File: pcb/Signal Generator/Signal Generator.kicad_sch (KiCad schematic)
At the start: 16 parts, among them SW1 SW_Push, SW1 SW_SPDT, U1 STM32F103CBTx, Y1 TG2520SMN_16.0000M-MCGNNM0

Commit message: Updated pcb
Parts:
- removed C9: 1u, symbol Device:C
- removed FB1: FerriteBead, symbol Device:FerriteBead
- removed U1: STM32F103CBTx, Package_QFP:LQFP-48_7x7mm_P0.5mm, symbol MCU_ST_STM32F1:STM32F103CBTx
- added C? (x2): 1u, symbol Device:C
- added R?: 10K, symbol Device:R
- added R? (x6): R, symbol Device:R
- added R?: 100K, symbol Device:R
- added U1: STM32F071RBTx, Package_QFP:LQFP-64_10x10mm_P0.5mm, symbol MCU_ST_STM32F0:STM32F071RBTx
- added U? (x3): Opamp_Dual, symbol Device:Opamp_Dual
- added U?: TS972IYQT, Signal Generator Components:TS972IYQT, symbol Signal Generator Components:TS972IYQT
- added U?: LDLN030G33R, Signal Generator Components:LDLN030G33R, symbol Signal Generator Components:LDLN030G33R
- C10: value C -> 100n
- C?: renamed from C6; value 4.5u -> 4.7u
- C?: renamed from C5; value 100n -> 4.7u
- renumbered C3 to C?, C4 to C?, C2 to C?, C1 to C?, C7 to C?, C8 to C?
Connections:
- net +3.3VA is gone; now on net +3.3V: C?.1, C?.1
- net +3.3V: now also C?.1, R?.2, R?.2, R?.2, U1.1 (VBAT), U1.13 (VDDA), U1.19 (VDD), U1.32 (VDD), U1.48 (VDDIO2), U1.64 (VDD), U?.5 (OUT), U?.8 (V+)
- net +5V: now also C?.1, R?.2, U?.1 (IN)
- net BOOT0: now also U1.60 (BOOT0)
- net DAC1: now also R?.1, U1.20 (PA4), U?.2 (-)
- net DAC2: now also R?.1, U1.21 (PA5), U?.6 (-)
- net GND: now also C?.2, C?.2, R?.1, R?.1, U1.12 (VSSA), U1.18 (VSS), U1.31 (VSS), U1.47 (VSS), U1.63 (VSS), U?.2 (GND), U?.4 (V-)
- net NRST: now also U1.7 (NRST)
- net OSC_IN: now also U1.5 (PF0)
- net UART1_RX: now also U1.59 (PB7)
- net UART1_TX: now also U1.58 (PB6)
- new net: R?.1, U?.3 (EN)
- new net: R?.1, R?.2, U?.5 (+)
- new net: R?.1, R?.2, U?.3 (+)
- new net: R?.1, U?.4 (PG)
- new net DAC1_OUT: R?.2, R?.2, U?.1, U?.7
- no-connect marks 1 -> 0
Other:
- sheet USB Plugs1 ports: added none; removed USB1_D+, USB1_D-
- note added: "LDO & Decoupling"
- note added: "When buffer is off: DAC output resistance 15k max Output speed follows the RC constant When internal buffer is on: OpAmp configured as an inverting amplifier DAC output resistance almost zero Speed determined by the buffer: T_settling = 4us max (250KHz) The most limiting factor when using only the internal DAC is the output impedance on the pin. To improve the DAC performance an external OpAmp ca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"
- note removed: "Decoupling"
- moved on the sheet: C?

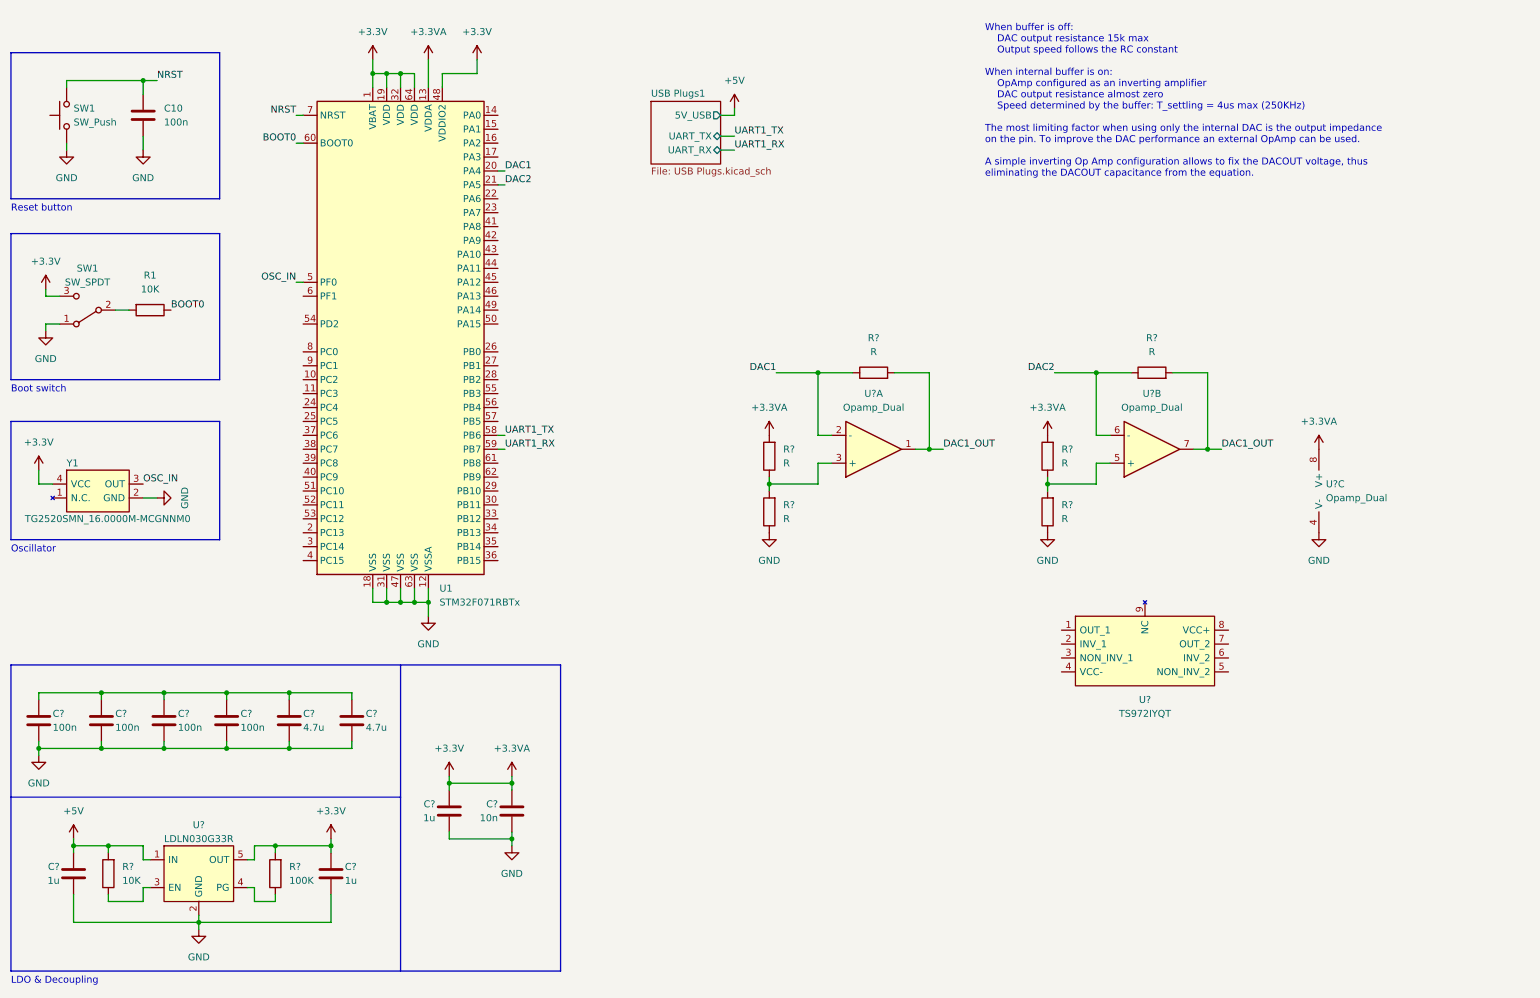
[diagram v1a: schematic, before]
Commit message: Updated schematic with almost final front end
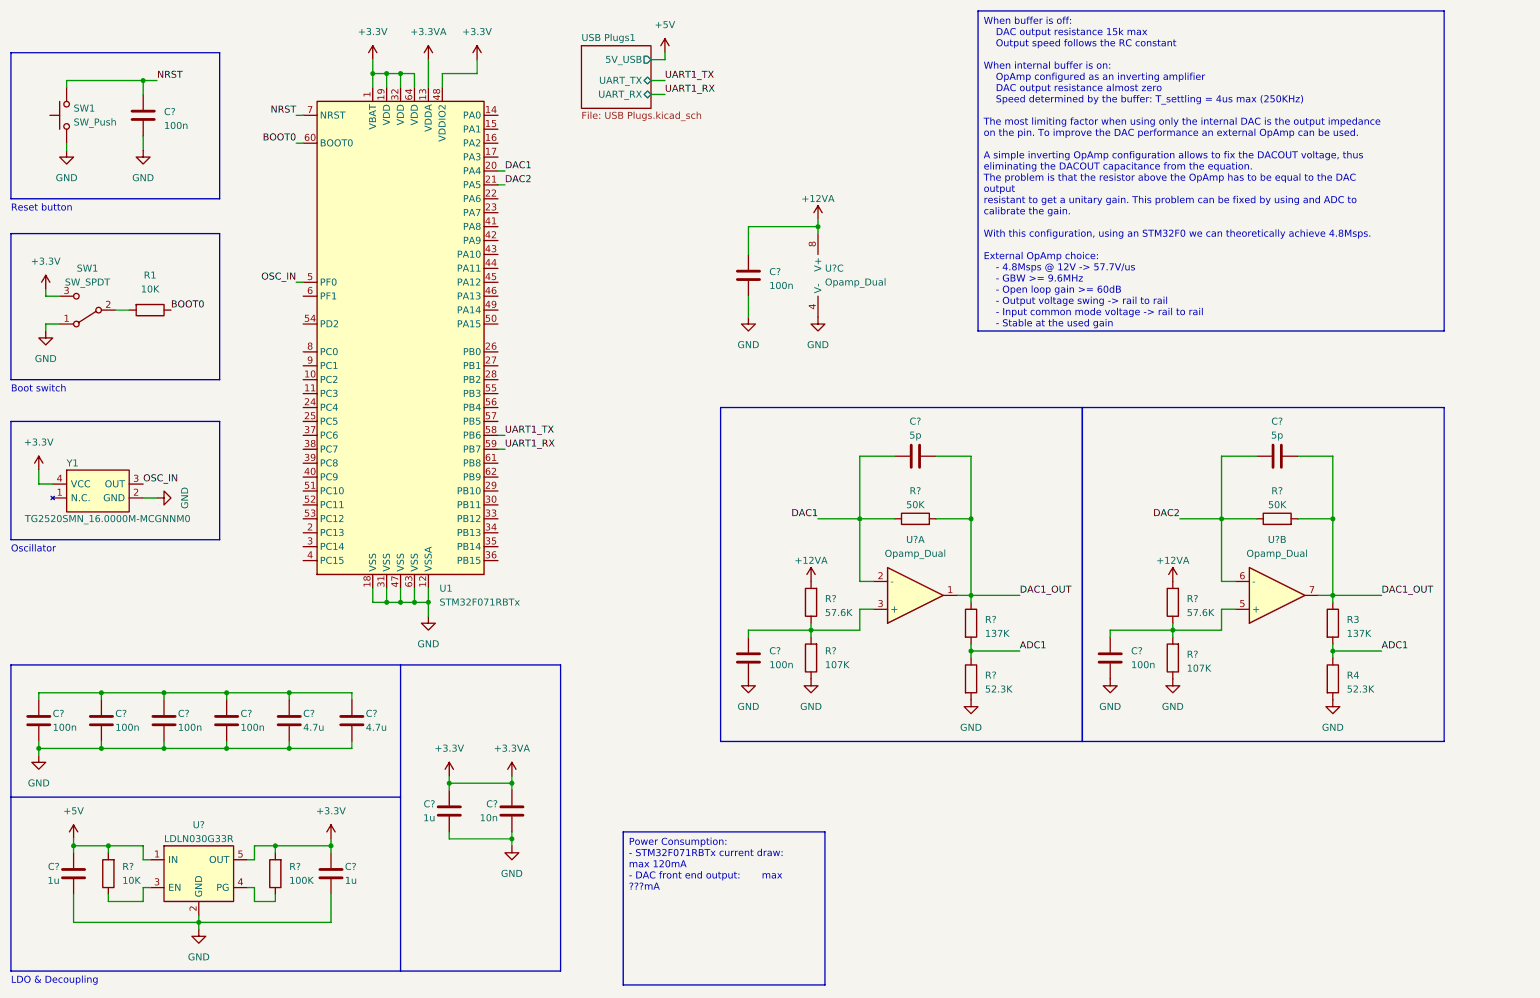
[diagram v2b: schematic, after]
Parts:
- removed U?: TS972IYQT, Signal Generator Components:TS972IYQT, symbol Signal Generator Components:TS972IYQT
- added C? (x3): 100n, symbol Device:C
- added C? (x2): 5p, symbol Device:C
- added R3, R?: 137K, symbol Device:R
- added R4, R?: 52.3K, symbol Device:R
- R? (x2): value R -> 50K
- R? (x2): value R -> 57.6K
- R? (x2): value R -> 107K
- renumbered C10 to C?
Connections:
- net +3.3V: no longer R?.2, R?.2, U?.8 (V+)
- net DAC1: now also C?.2
- net DAC1_OUT: now also C?.1, C?.2, R3.1, R?.1
- net DAC2: now also C?.1
- net GND: now also C?.2, C?.2, C?.2, R4.2, R?.2
- net at R?.1, R?.2, U?.5 (+): now also C?.1
- net at R?.1, R?.2, U?.3 (+): now also C?.1
- new net +12VA: C?.1, R?.2, R?.2, U?.8 (V+)
- new net ADC1: R3.2, R4.1, R?.1, R?.2
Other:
- note removed: "When buffer is off: DAC output resistance 15k max Output speed follows the RC constant When internal buffer is on: OpAmp configured as an inverting amplifier DAC output resistance almost zero Speed determined by the buffer: T_settling = 4us max (250KHz) The most limiting factor when using only the internal DAC is the output impedance on the pin. To improve the DAC performance an external OpAmp ca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"
- moved on the sheet: R?, U?A, U?B, U?C
